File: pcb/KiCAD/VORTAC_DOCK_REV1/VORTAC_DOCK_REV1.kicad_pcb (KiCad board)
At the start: 4 copper layers, 25.4 x 16.4 mm, 24 parts, among them J1 Conn_01x05, J3 Screw_Terminal_01x02, J5 Conn_01x04, U1 WS2811, U2 TPS26630RGE, U6 AP63205WU

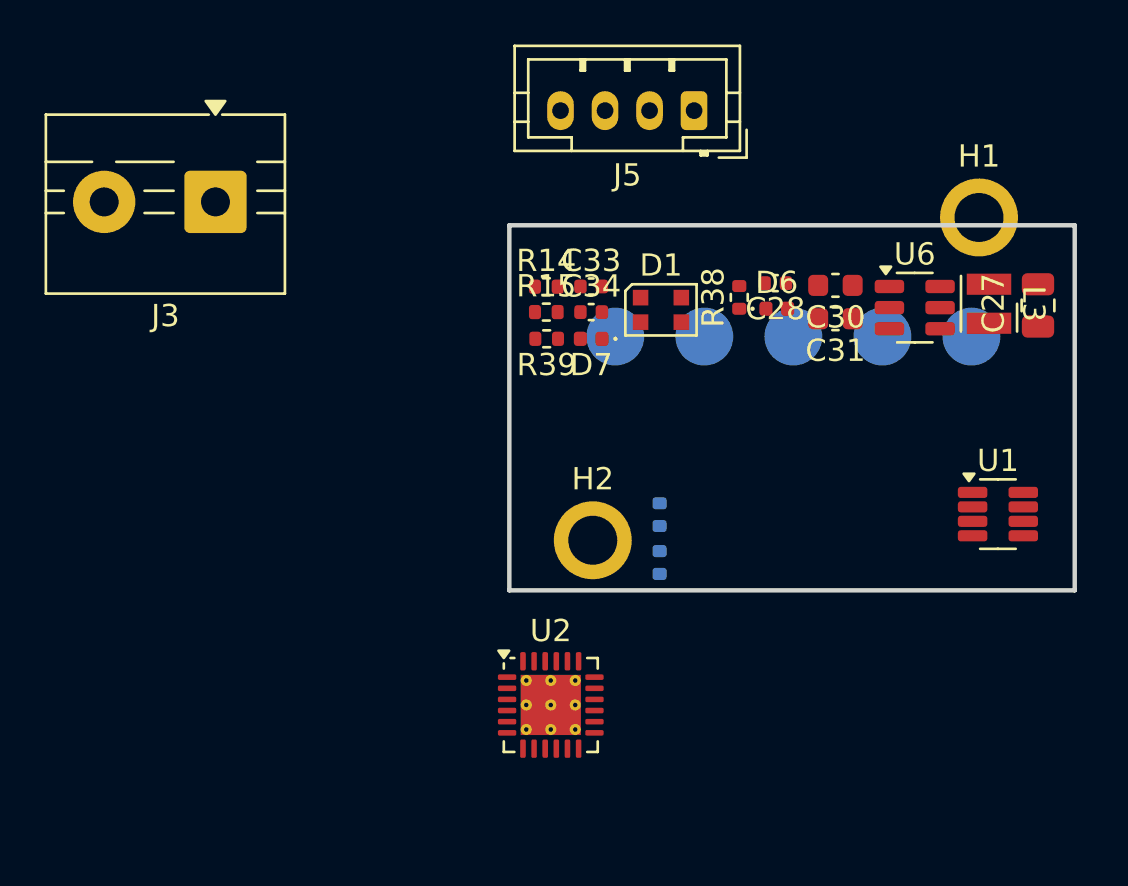
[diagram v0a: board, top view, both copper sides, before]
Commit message: new Footprints and replaced chonky connectors
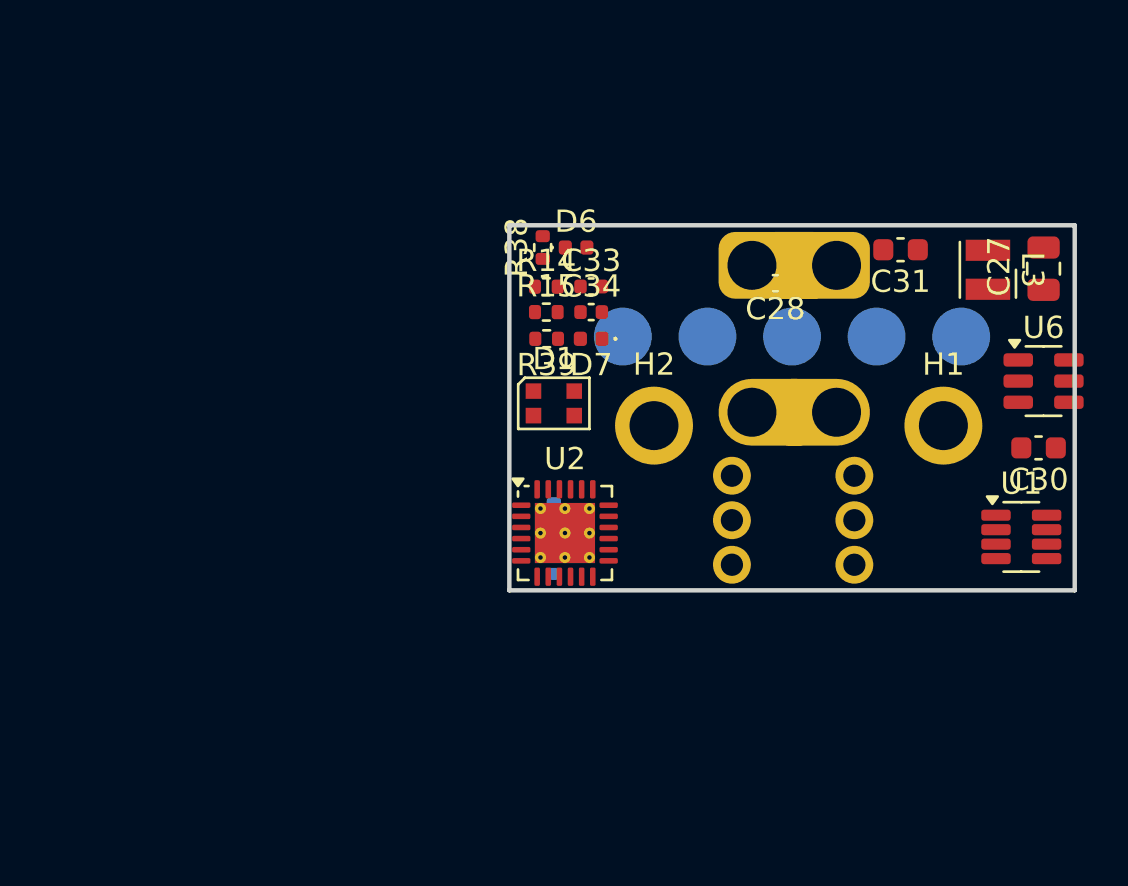
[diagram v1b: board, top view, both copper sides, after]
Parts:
- removed J3: Screw_Terminal_01x02, TerminalBlock:TerminalBlock_MaiXu_MX126-5.0-02P_1x02_P5.00mm
- removed J5: Conn_01x04, Connector_JST:JST_PH_B4B-PH-K_1x04_P2.00mm_Vertical
- added J10: Conn_01x03, Vortac:Solderpoint_01x03_Data, F.Cu at (115.5, 109.2)
- added J7: Conn_01x01, Vortac:Dock_Solderpoint_02x01_GND, F.Cu at (112.8, 99.8)
- added J8: Conn_01x01, Vortac:Dock_Solderpoint_02x01_VCC, F.Cu at (112.8, 106.4)
- added J9: Conn_01x03, Vortac:Solderpoint_01x03_Data, F.Cu at (110.0, 109.2)
- moved C30 11.7 mm to (123.8, 108.0)
- moved H1 9.49 mm to (119.5, 107.0)
- moved D6 9.43 mm to (103.0, 99.0)
- moved R38 9.11 mm to (101.5, 99.0)
- moved J1 7.94 mm to (112.7, 103.0)
- moved U2 7.75 mm to (102.5, 111.8)
- moved U6 6.66 mm to (124.0, 105.0)
- moved D1 6.39 mm to (102.0, 106.0)
- moved H2 5.84 mm to (106.5, 107.0)
- moved R12 4.75 mm to (102.0, 113.2)
- moved R13 4.75 mm to (102.0, 111.0)
- moved C31 4.26 mm to (117.6, 99.1)
- moved C27 1.67 mm to (124.0, 100.0)
- moved L3 1.53 mm to (121.5, 100.0)
- moved U1 1.47 mm to (123.0, 112.0)

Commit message: Vortac Dock rough component placement #NO-JIRA
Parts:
- removed D1: NeoPixel_THT, LED_SMD:LED_WS2812B-2020_PLCC4_2.0x2.0mm
- added JP1: SolderJumper_2_Open, Vortac:SolderJumper_Hex_Open_Pad, F.Cu at (89.7, 106.7)
- added JP2: SolderJumper_2_Open, Jumper:SolderJumper-2_P1.3mm_Open_RoundedPad1.0x1.5mm, F.Cu at (93.3, 106.7)
- added R16: 120R, Resistor_SMD:R_0402_1005Metric, F.Cu at (89.0, 110.2)
- R12, R13: moved to F.Cu
- moved D6 23.5 mm to (111.2, 121.0), turned to 180 degrees
- moved D7 23.4 mm to (88.7, 121.2)
- moved R38 23.1 mm to (111.2, 120.0), turned to 0 degrees
- moved R39 21.4 mm to (88.7, 120.1), turned to 0 degrees
- moved C30 19.0 mm to (104.8, 106.5), turned to -90 degrees
- moved L3 18.4 mm to (105.8, 109.6)
- moved C27 17.9 mm to (108.8, 109.5), turned to 0 degrees
- moved U1 17.5 mm to (107.5, 120.0)
- moved H2 16.2 mm to (91.7, 113.7)
- moved R14 15.9 mm to (95.1, 115.2)
- moved R15 15.8 mm to (95.0, 116.2)
- moved C33 15.6 mm to (95.1, 113.8)
- moved R13 15.0 mm to (88.6, 117.7), turned to 0 degrees
- moved U6 15.0 mm to (109.1, 106.8)
- moved J10 14.9 mm to (102.5, 116.6)
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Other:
- board size 25.4 x 16.4 mm -> 25.2 x 18 mm

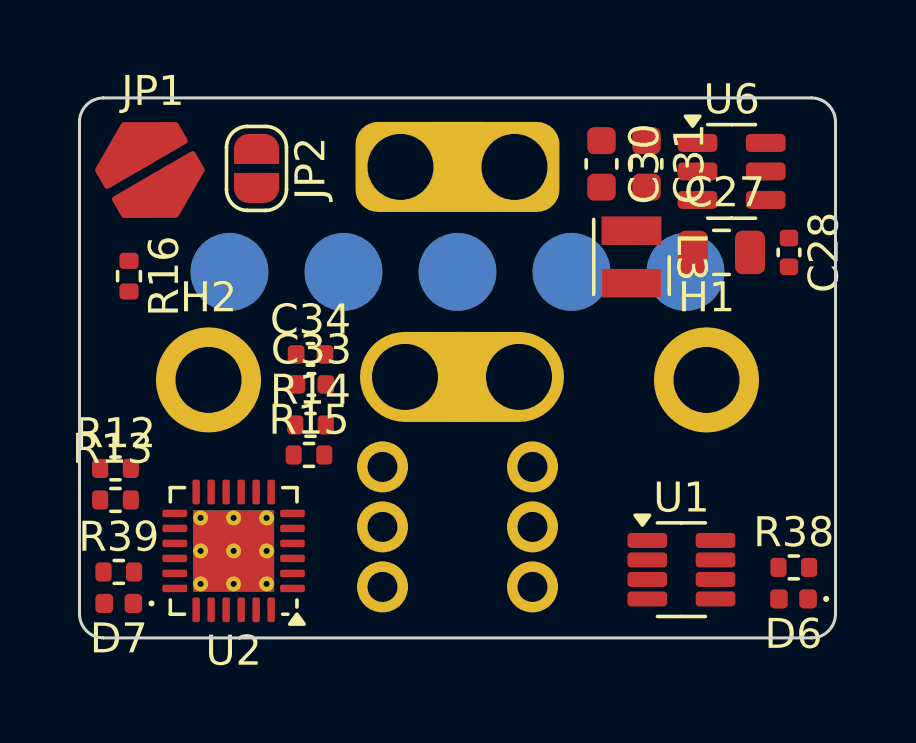
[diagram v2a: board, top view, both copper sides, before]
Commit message: Updated PCB Outline and Refferences based on CAD
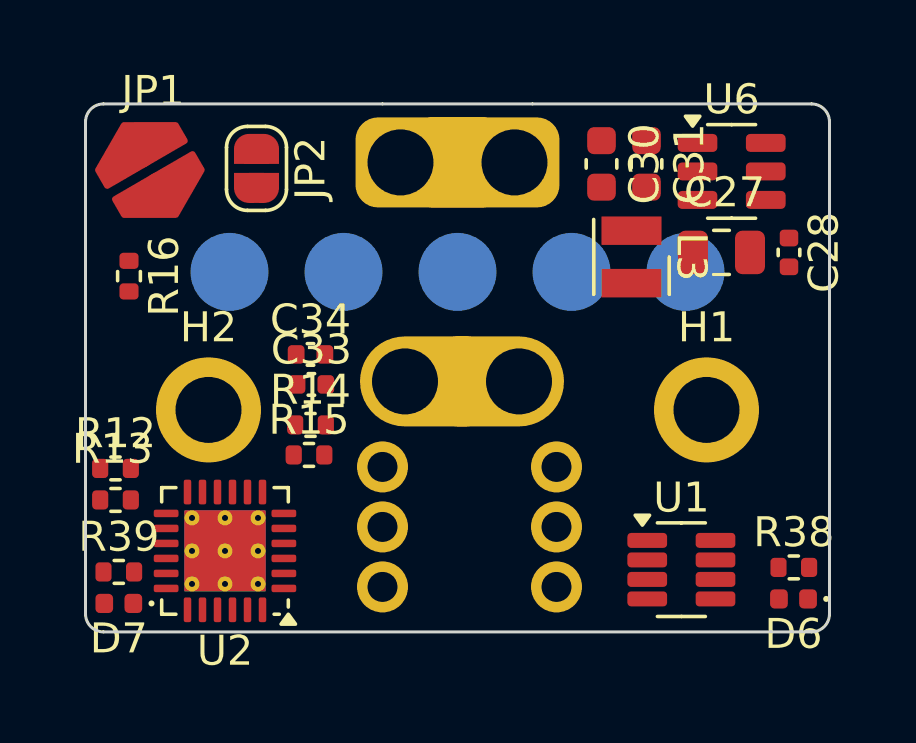
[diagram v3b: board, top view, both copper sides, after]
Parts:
- moved H1 1.00 mm to (108.3, 114.7)
- moved H2 1.00 mm to (91.7, 114.7)
- moved J10 0.80 mm to (103.3, 116.6)
- moved U2 0.29 mm to (92.2, 119.4)
- moved J8 0.15 mm to (100.2, 113.8)
- moved J7 0.15 mm to (100.0, 106.5)
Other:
- board size 25.2 x 18 mm -> 24.8 x 17.6 mm

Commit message: Routed Vortac Dock PCB REV1
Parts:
- removed JP2: SolderJumper_2_Open, Jumper:SolderJumper-2_P1.3mm_Open_RoundedPad1.0x1.5mm
- JP1: footprint Vortac:SolderJumper_Hex_Open_Pad -> Jumper:SolderJumper-2_P1.3mm_Open_RoundedPad1.0x1.5mm
- R4: renamed from R15; value 170K -> 165K
- U3: renamed from U2; footprint Package_DFN_QFN:Texas_RGE0024H_VQFN-24-1EP_4x4mm_P0.5mm_EP2.7x2.7mm_ThermalVias -> Vortac:Texas_RGE0024H_VQFN-24-1EP_4x4mm_P0.5mm_EP2.7x2.7mm_ThermalVias
- moved JP1 24.5 mm to (110.6, 119.4), turned to 90 degrees
- moved R1 22.4 mm to (88.8, 118.4)
- moved D1 22.4 mm to (88.8, 119.3)
- moved R3 21.9 mm to (108.8, 119.5), turned to 90 degrees
- moved U2 15.0 mm to (92.5, 120.2)
- moved U3 12.3 mm to (91.3, 107.1), turned to 0 degrees
- moved R4 8.47 mm to (94.5, 107.8), turned to -90 degrees
- moved C5 7.93 mm to (88.2, 109.0), turned to -90 degrees
- moved R6 7.57 mm to (91.8, 110.8), turned to -90 degrees
- moved J4 6.80 mm to (96.5, 116.5)
- moved C1 6.03 mm to (105.6, 106.9), turned to 90 degrees
- moved J5 6.00 mm to (103.5, 116.5)
- moved C2 5.75 mm to (110.0, 108.8), turned to 0 degrees
- moved R5 5.60 mm to (94.5, 109.6), turned to -90 degrees
- moved C3 5.37 mm to (110.0, 110.3), turned to 0 degrees
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- renumbered C28 to C1, C30 to C2, C31 to C3, C27 to C4, C34 to C5, C33 to C6, D6 to D1, D7 to D2, J7 to J1, J8 to J2, J1 to J3, J10 to J4, J9 to J5, L3 to L1, R38 to R1, R39 to R2, R16 to R3, R14 to R5, R13 to R6, R12 to R7, U6 to U1, U1 to U2
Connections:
- J3 pad 1: VDC_SW -> TOOL_ID
- J3 pad 2: TOOL_ID -> VDC_SW
- J4 pad 1: CAN_H -> CAN_L
- J4 pad 2: CAN_L -> CAN_H
- J5 pad 1: CAN_H -> CAN_L
- J5 pad 2: CAN_L -> CAN_H
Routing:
- net CAN_L: track 0.00 -> 25.1 mm
- net CAN_H: track 0.00 -> 24.6 mm
- net LED_FLT_DRAIN: track 0.00 -> 18.7 mm
- net +5V: track 0.00 -> 16.0 mm, vias 0 -> 4
- net EFUSE_SHDN: track 0.00 -> 12.9 mm
- net TOOL_ID: track 0.00 -> 11.2 mm, vias 0 -> 1
- net WS2811_DO: track 0.00 -> 10.5 mm
- net /+5V_OUT: track 0.00 -> 4.67 mm
- net VDC: track 0.00 -> 3.65 mm, vias 0 -> 6
- net WS2811_DIN: track 0.00 -> 2.94 mm
- net Net-(U3-PGTH): track 0.00 -> 2.58 mm
- net LED_0_DRAIN: track 0.00 -> 2.33 mm
- net Net-(JP1-A): track 0.00 -> 1.78 mm
- net /+5V_BST: track 0.00 -> 1.38 mm
- net Net-(U3-ILIM): track 0.00 -> 1.36 mm
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- added copper zone on In1.Cu, net +5V
- added copper zone on In2.Cu, net +5V
- added copper zone on B.Cu, net GND
- added copper zone on F.Cu, net GND
- added copper zone on F.Cu, net VDC
- added copper zone on In1.Cu, net VDC
- added copper zone on In2.Cu, net VDC
- added copper zone on B.Cu, net VDC_SW
- added copper zone on F.Cu, net VDC_SW
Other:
- board text added: "CH"
- board text added: "CL"
- board text added: "DO"

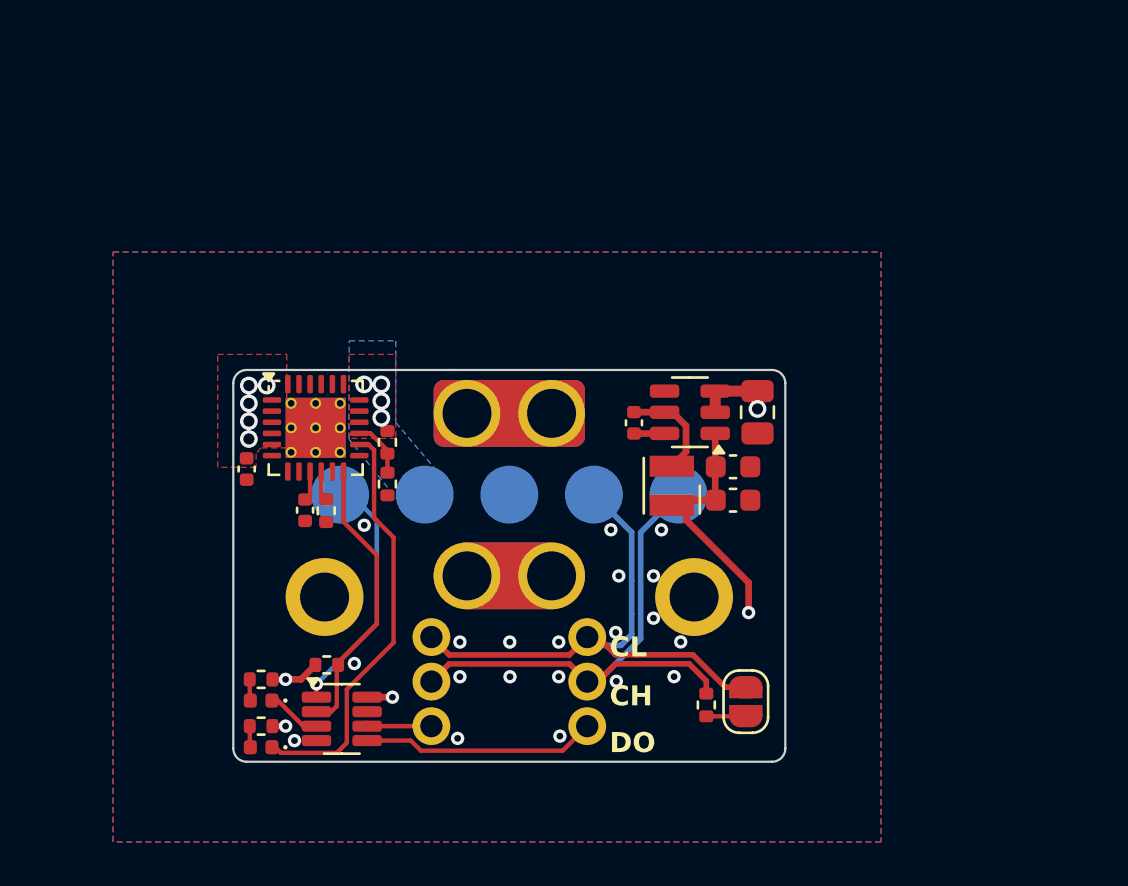
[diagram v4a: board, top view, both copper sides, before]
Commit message: Added VORTAC_TOOLPLATE_REV2
Modified VORTAC_TOOL
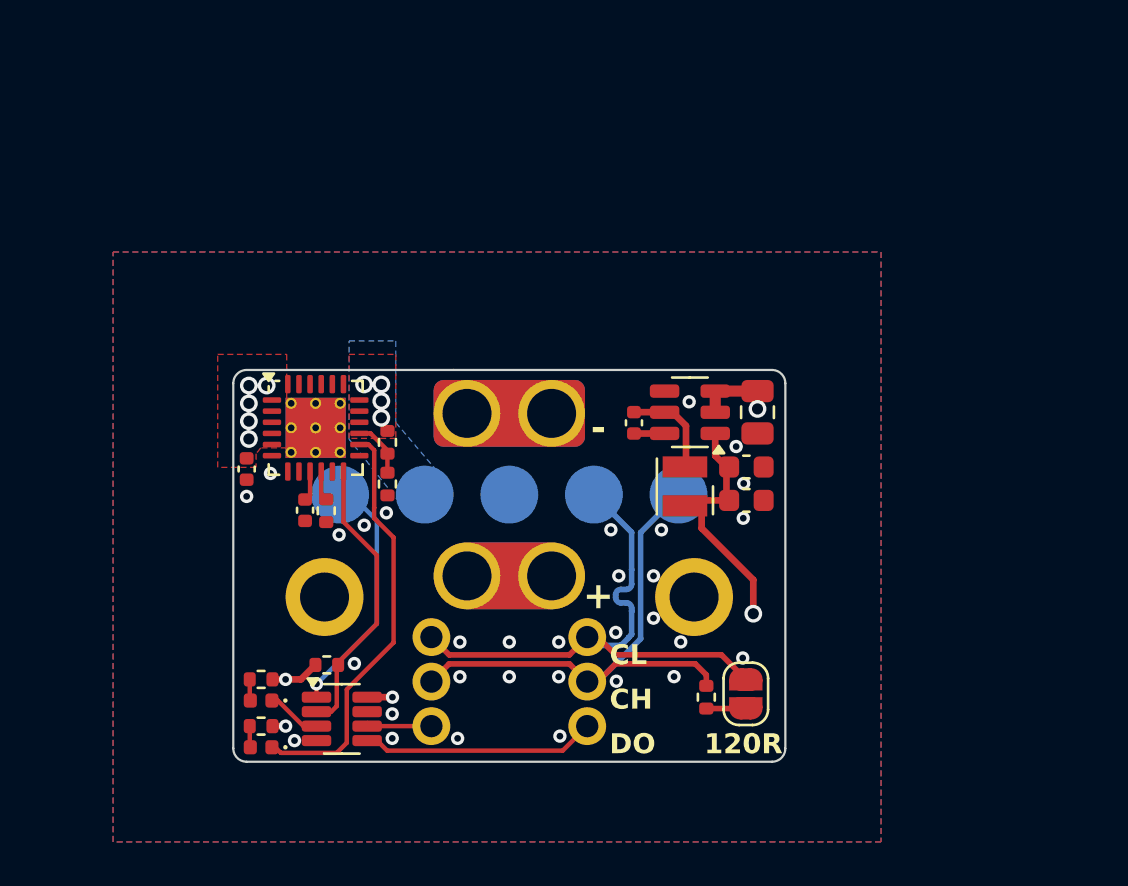
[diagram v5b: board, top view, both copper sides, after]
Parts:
- moved C2 0.60 mm to (110.7, 108.9)
- moved C3 0.60 mm to (110.7, 110.4)
- moved L1 0.59 mm to (107.9, 109.7)
- moved JP1 0.35 mm to (110.6, 119.0)
- moved R3 0.35 mm to (108.8, 119.2)
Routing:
- net +5V: track 16.0 -> 14.8 mm
- net CAN_L: track 25.1 -> 25.9 mm
- net GND: vias 20 -> 31
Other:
- board text added: "+"
- board text added: "-"
- board text added: "120R"

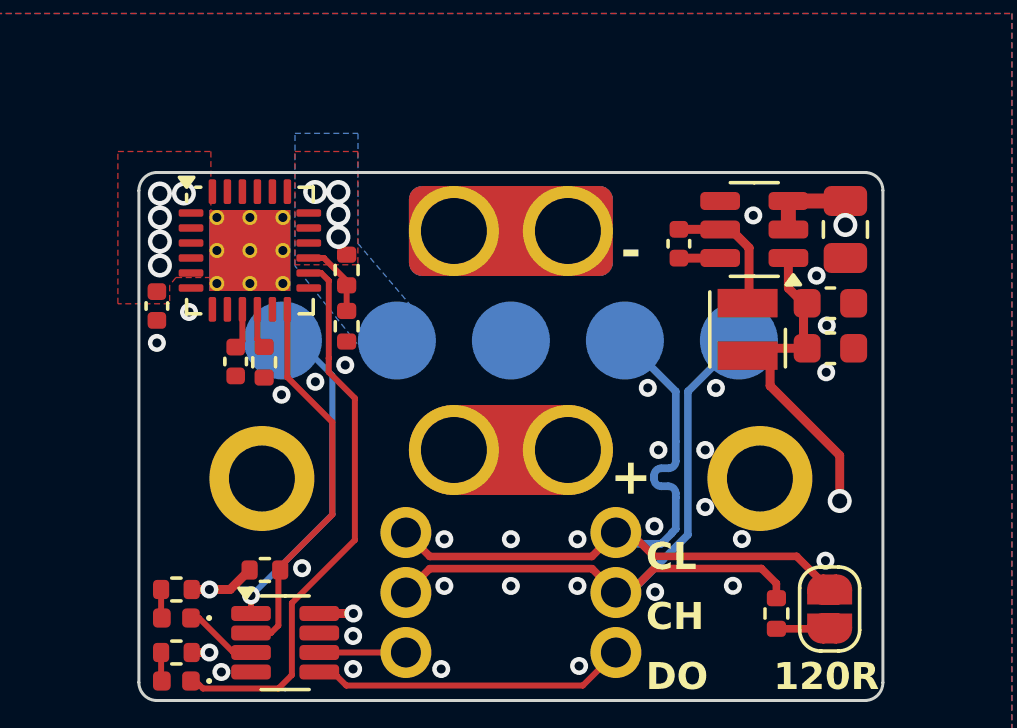
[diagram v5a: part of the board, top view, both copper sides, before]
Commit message: (Hopefully) Finalized DOCK, TOOL and TOOLPLATE REV2 for ordering
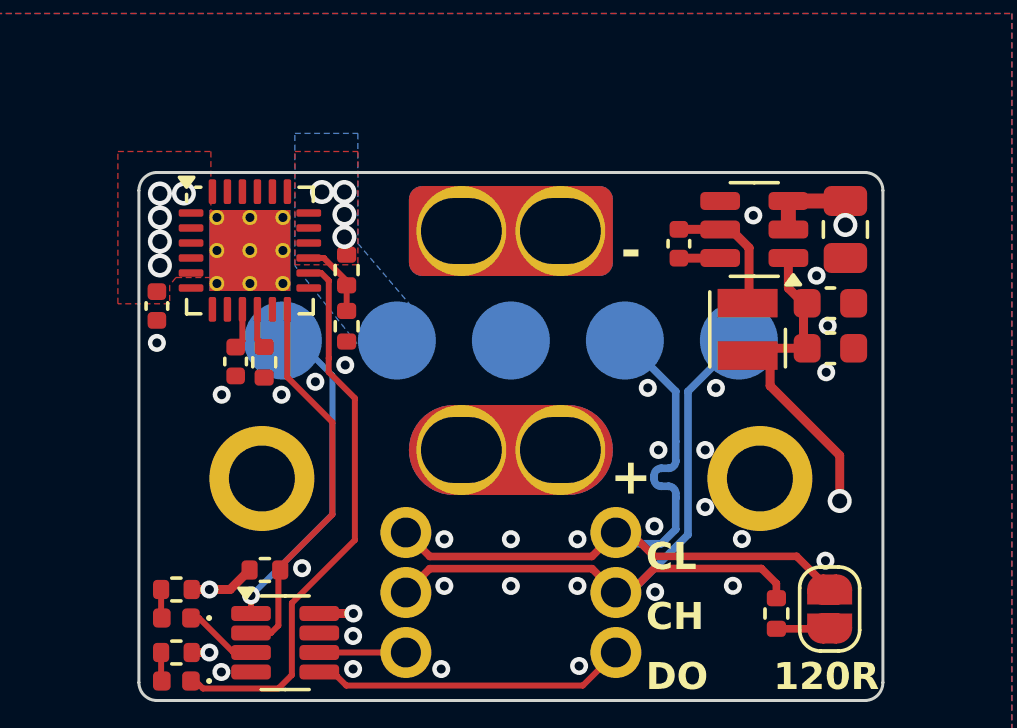
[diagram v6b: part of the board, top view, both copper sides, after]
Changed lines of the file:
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@@
 		)
 		(pad "1" thru_hole circle
-			(at -1.9 0)
+			(at -1.65 0)
 			(size 3 3)
-			(drill 2.2)
+			(drill oval 2.7 2.2)
 			(layers "*.Cu")
 			(remove_unused_layers no)
@@
 		)
 		(pad "1" thru_hole circle
-			(at 1.9 0)
+			(at 1.65 0)
 			(size 3 3)
-			(drill 2.2)
+			(drill oval 2.7 2.2)
 			(layers "*.Cu")
 			(remove_unused_layers no)
@@
 		)
 		(pad "1" thru_hole circle
-			(at -1.9 0)
+			(at -1.65 0)
 			(size 3 3)
-			(drill 2.2)
+			(drill oval 2.7 2.2)
 			(layers "*.Cu")
 			(remove_unused_layers no)
@@
 		)
 		(pad "1" thru_hole circle
-			(at 1.9 0)
+			(at 1.65 0)
 			(size 3 3)
-			(drill 2.2)
+			(drill oval 2.7 2.2)
 			(layers "*.Cu")
 			(remove_unused_layers no)
@@
 	)
 	(segment
-		(start 105.022431 116.868528)
-		(end 105.006472 116.868528)
-		(width 0.254)
-		(layer "B.Cu")
-		(net 4)
-	)
-	(segment
-		(start 105.361015 116.513985)
-		(end 105.361015 116.529944)
+		(start 105.495 116.395959)
+		(end 105.495 115.35)
 		(width 0.254)
 		(layer "B.Cu")
@@
 	)
 	(segment
-		(start 105 116.875)
-		(end 103.875 116.875)
-		(width 0.254)
-		(layer "B.Cu")
-		(net 4)
-	)
-	(segment
 		(start 105.255 114.360006)
 		(end 105.014979 114.360006)
@@
 	)
 	(segment
-		(start 103.875 116.875)
-		(end 103.5 116.5)
-		(width 0.254)
-		(layer "B.Cu")
-		(net 4)
-	)
-	(segment
 		(start 105.014979 114.960006)
 		(end 105.255 114.960006)
@@
 	)
 	(segment
-		(start 105.495 116.38)
-		(end 105.361015 116.513985)
-		(width 0.254)
-		(layer "B.Cu")
-		(net 4)
-	)
-	(segment
 		(start 105.495 115.200006)
 		(end 105.495 115.320006)
@@
 	)
 	(segment
-		(start 105.495 115.35)
-		(end 105.495 116.38)
+		(start 103.5 116.5)
+		(end 103.875 116.875)
 		(width 0.254)
 		(layer "B.Cu")
@@
 	)
 	(segment
-		(start 105.006472 116.868528)
-		(end 105 116.875)
+		(start 103.875 116.875)
+		(end 105.015959 116.875)
 		(width 0.254)
 		(layer "B.Cu")
@@
 	)
 	(segment
-		(start 105.361015 116.529944)
-		(end 105.022431 116.868528)
+		(start 105.015959 116.875)
+		(end 105.495 116.395959)
 		(width 0.254)
 		(layer "B.Cu")
@@
 	)
 	(via
-		(at 94.25 105.9)
+		(at 94.45 105.9)
 		(size 0.8)
 		(drill 0.5)
@@
 	)
 	(via
-		(at 94.25 106.65)
+		(at 94.45 106.65)
 		(size 0.8)
 		(drill 0.5)
@@
 	)
 	(via
-		(at 93.475 105.15)
+		(at 93.7 105.15)
 		(size 0.8)
 		(drill 0.5)
@@
 	)
 	(via
-		(at 94.25 105.15)
+		(at 94.45 105.15)
 		(size 0.8)
 		(drill 0.5)
@@
 	)
 	(via
-		(at 89.27 109.15)
+		(at 90.36 111.907139)
 		(size 0.6)
 		(drill 0.3)
@@
 	)
 	(via
-		(at 110.53 109.6)
+		(at 110.56 109.61)
 		(size 0.6)
 		(drill 0.3)
